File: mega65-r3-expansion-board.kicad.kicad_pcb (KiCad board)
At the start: 4 copper layers, 215 x 126.9 mm, 99 parts, among them J1 Conn_01x04, J10 PMOD2, J11 Conn_02x05_Odd_Even, J12 Conn_02x17_Odd_Even, J13 Conn_02x17_Odd_Even, J14 Component A/V, J15 ESP32 Connector, J2 Conn_01x04, J3 C64_User_Port, J4 Mini-DIN-8-With-Shield, J5 C64_Tape_Port, J6 OKR-T/3-W12-C, J7 Conn_02x06_Odd_Even, J8 Conn_02x06_Odd_Even, J9 PMOD1, U1 74HC595, U10 74LS125, U11 74HC595, U12 74LS125, U13 74LS125, U2 74LVC165, U3 74LS125, U4 74HC595, U5 74LVC165, U6 74HC595, U7 74LVC165, U8 74LS125, U9 74LS125

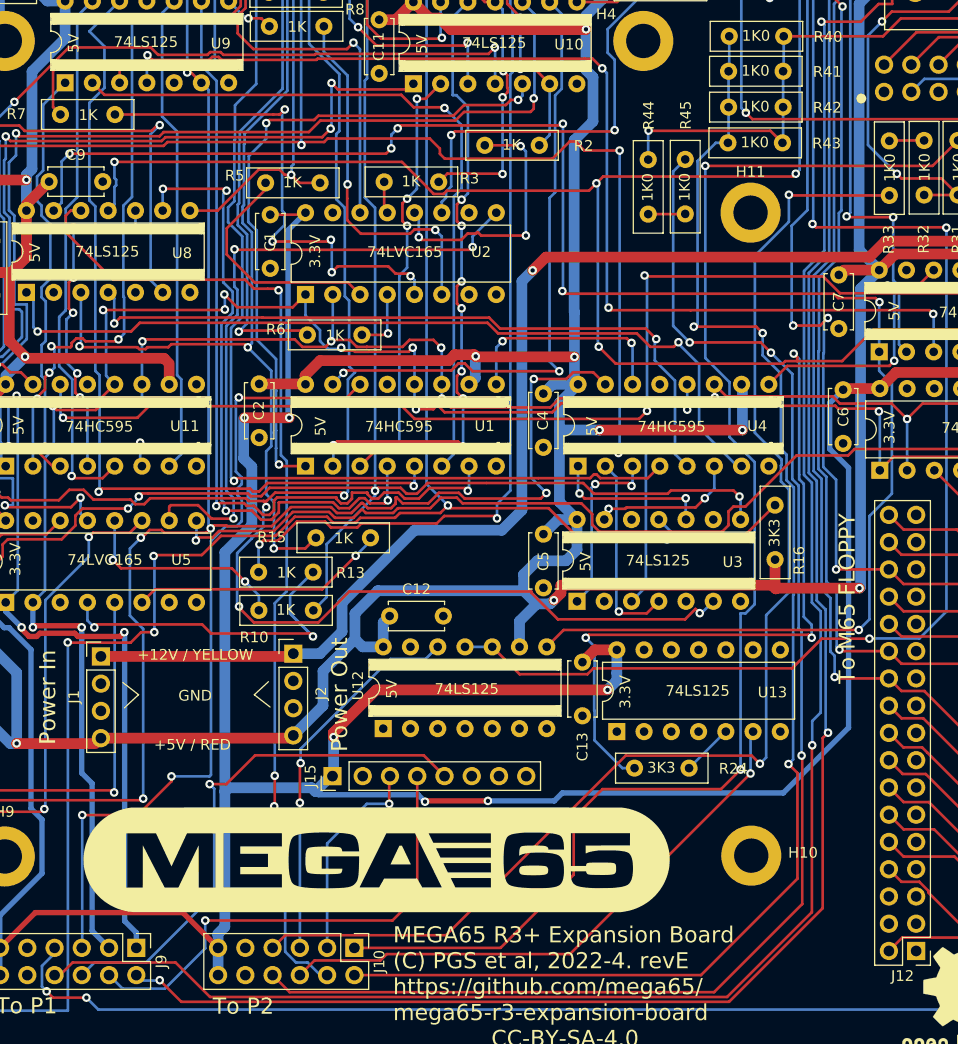
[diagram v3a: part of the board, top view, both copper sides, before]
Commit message: begin peeling out C1565 port to separate sheet
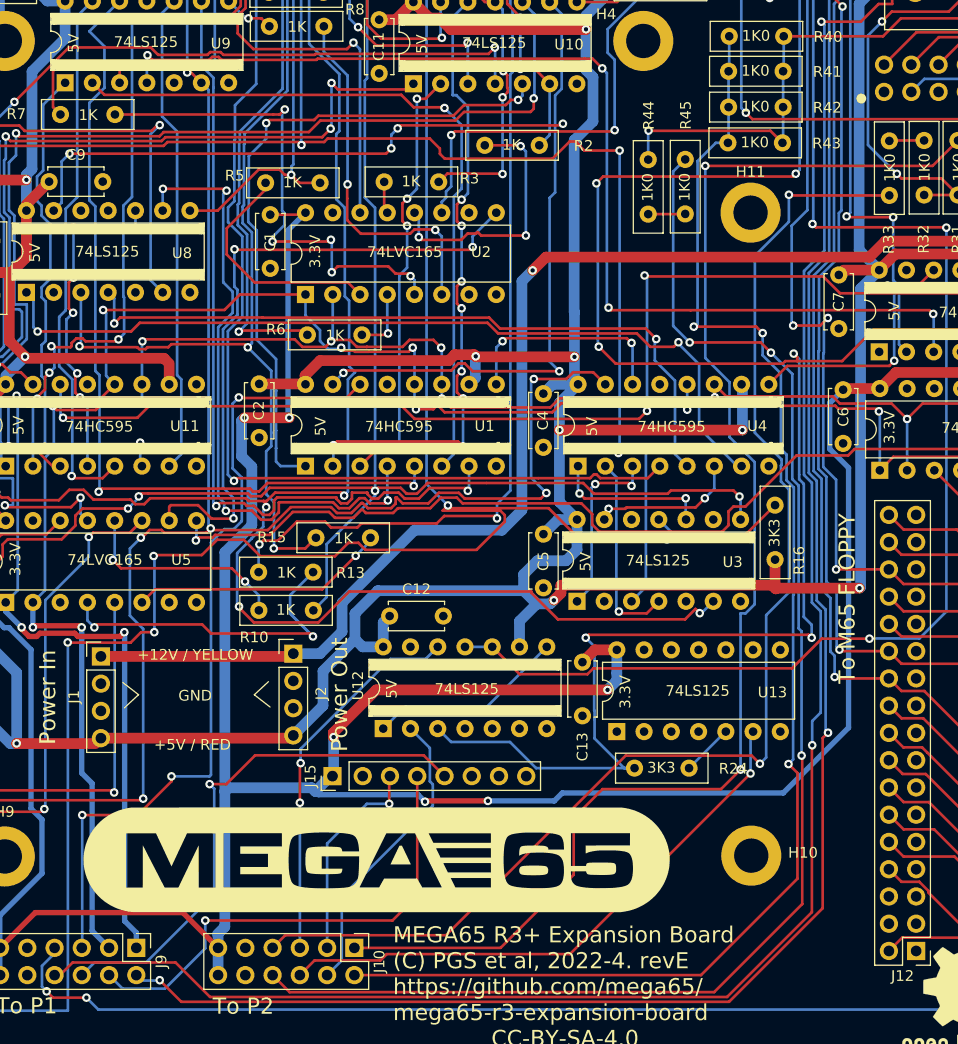
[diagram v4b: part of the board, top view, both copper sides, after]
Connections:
- net /User Port, Tape Port & C1565 Port/6V_REG_CTL renamed /User Port & Tape Port/6V_REG_CTL
- net /User Port, Tape Port & C1565 Port/ATN_O renamed /User Port & Tape Port/ATN_O
- net /User Port, Tape Port & C1565 Port/CNT1 renamed /User Port & Tape Port/CNT1
- net /User Port, Tape Port & C1565 Port/CNT1_O renamed /User Port & Tape Port/CNT1_O
- net /User Port, Tape Port & C1565 Port/CNT2 renamed /User Port & Tape Port/CNT2
- net /User Port, Tape Port & C1565 Port/CNT2_O renamed /User Port & Tape Port/CNT2_O
- net /User Port, Tape Port & C1565 Port/DATA_0 renamed /User Port & Tape Port/DATA_0
- net /User Port, Tape Port & C1565 Port/DATA_0_O renamed /User Port & Tape Port/DATA_0_O
- net /User Port, Tape Port & C1565 Port/DATA_1 renamed /User Port & Tape Port/DATA_1
- net /User Port, Tape Port & C1565 Port/DATA_1_O renamed /User Port & Tape Port/DATA_1_O
- net /User Port, Tape Port & C1565 Port/DATA_2 renamed /User Port & Tape Port/DATA_2
- net /User Port, Tape Port & C1565 Port/DATA_2_O renamed /User Port & Tape Port/DATA_2_O
- net /User Port, Tape Port & C1565 Port/DATA_3 renamed /User Port & Tape Port/DATA_3
- net /User Port, Tape Port & C1565 Port/DATA_3_O renamed /User Port & Tape Port/DATA_3_O
- net /User Port, Tape Port & C1565 Port/DATA_4 renamed /User Port & Tape Port/DATA_4
- net /User Port, Tape Port & C1565 Port/DATA_4_O renamed /User Port & Tape Port/DATA_4_O
- net /User Port, Tape Port & C1565 Port/DATA_5 renamed /User Port & Tape Port/DATA_5
- net /User Port, Tape Port & C1565 Port/DATA_5_O renamed /User Port & Tape Port/DATA_5_O
- net /User Port, Tape Port & C1565 Port/DATA_6 renamed /User Port & Tape Port/DATA_6
- net /User Port, Tape Port & C1565 Port/DATA_6_O renamed /User Port & Tape Port/DATA_6_O
- net /User Port, Tape Port & C1565 Port/DATA_7 renamed /User Port & Tape Port/DATA_7
- net /User Port, Tape Port & C1565 Port/DATA_7_O renamed /User Port & Tape Port/DATA_7_O
- net /User Port, Tape Port & C1565 Port/EN_DATA_0 renamed /User Port & Tape Port/EN_DATA_0
- net /User Port, Tape Port & C1565 Port/EN_DATA_1 renamed /User Port & Tape Port/EN_DATA_1
- net /User Port, Tape Port & C1565 Port/EN_DATA_2 renamed /User Port & Tape Port/EN_DATA_2
- net /User Port, Tape Port & C1565 Port/EN_DATA_3 renamed /User Port & Tape Port/EN_DATA_3
- net /User Port, Tape Port & C1565 Port/EN_DATA_4 renamed /User Port & Tape Port/EN_DATA_4
- net /User Port, Tape Port & C1565 Port/EN_DATA_5 renamed /User Port & Tape Port/EN_DATA_5
- net /User Port, Tape Port & C1565 Port/EN_DATA_6 renamed /User Port & Tape Port/EN_DATA_6
- net /User Port, Tape Port & C1565 Port/EN_DATA_7 renamed /User Port & Tape Port/EN_DATA_7
- net /User Port, Tape Port & C1565 Port/EN_PA2 renamed /User Port & Tape Port/EN_PA2
- net /User Port, Tape Port & C1565 Port/FLAG2 renamed /User Port & Tape Port/FLAG2
- net /User Port, Tape Port & C1565 Port/PA2 renamed /User Port & Tape Port/PA2
- net /User Port, Tape Port & C1565 Port/PC2 renamed /User Port & Tape Port/PC2
- net /User Port, Tape Port & C1565 Port/RESET_N renamed /User Port & Tape Port/RESET_N
- net /User Port, Tape Port & C1565 Port/RESET_N_O renamed /User Port & Tape Port/RESET_N_O
- net /User Port, Tape Port & C1565 Port/SP1 renamed /User Port & Tape Port/SP1
- net /User Port, Tape Port & C1565 Port/SP1_O renamed /User Port & Tape Port/SP1_O
- net /User Port, Tape Port & C1565 Port/SP2 renamed /User Port & Tape Port/SP2
- net /User Port, Tape Port & C1565 Port/SP2_O renamed /User Port & Tape Port/SP2_O
- net /User Port, Tape Port & C1565 Port/TAPE_MOTOR renamed /User Port & Tape Port/TAPE_MOTOR
- net /User Port, Tape Port & C1565 Port/TAPE_READ renamed /User Port & Tape Port/TAPE_READ
- net /User Port, Tape Port & C1565 Port/TAPE_SENSE renamed /User Port & Tape Port/TAPE_SENSE
- net /User Port, Tape Port & C1565 Port/TAPE_WRITE renamed /User Port & Tape Port/TAPE_WRITE
- U12 pad 1: unconnected-(U12-Pad1) -> EN_1565_SERIO
- U12 pad 2: unconnected-(U12-Pad2) -> 1565_SERIO_O
- U12 pad 3: unconnected-(U12-Pad3) -> 1565_SERIO
- U6 pad 1: EN_1565_SERIO -> unconnected-(U6-QB-Pad1)
- U8 pad 11: 1565_SERIO -> unconnected-(U8-Pad11)
- U8 pad 12: 1565_SERIO_O -> unconnected-(U8-Pad12)
- U8 pad 13: EN_1565_SERIO -> unconnected-(U8-Pad13)
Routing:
- net EN_1565_SERIO: track 161.5 -> 18.4 mm, vias 7 -> 0
- net 1565_SERIO_O: track 92.7 -> 27.9 mm, vias 3 -> 0
- net unconnected-(U8-Pad13): track 0.00 -> 53.8 mm, vias 0 -> 4
- net 1565_SERIO: track 292.8 -> 261.7 mm, vias 11 -> 10
- net /User Port & Tape Port/CNT1: track 190.9 -> 204.1 mm
- net EXP_LATCH: track 202.8 -> 200.9 mm, vias 12 -> 10
- net /User Port & Tape Port/DATA_1_O: vias 3 -> 2
